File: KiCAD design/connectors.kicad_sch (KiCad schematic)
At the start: 6 parts

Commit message: finished conectors / sensors / converters
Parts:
- added J?: JST BATTERY, Connector_JST:JST_XH_B2B-XH-A_1x02_P2.50mm_Vertical, symbol Connector_Generic:Conn_01x02
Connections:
- net GND: now also J?.1 (Pin_1)
- new net +BATT: J?.2 (Pin_2)
- no-connect marks 9 -> 8
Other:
- note added: "BATTERY"
- company: (none) -> Oulu University
- title: (none) -> Connectors
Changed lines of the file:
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@@
 (kicad_sch (version 20211123) (generator eeschema)
   (paper "A4")
+  (title_block
+    (title "Connectors")
+    (company "Oulu University")
+  )
   (junction (at 50.8 38.1) (diameter 0) (color 0 0 0 0)
   )
@@
   (no_connect (at 38.1 45.72))
   (no_connect (at 50.8 43.18))
-  (no_connect (at 146.05 151.13))
   (no_connect (at 119.38 76.2))
   (no_connect (at 50.8 63.5))
@@
     (stroke (width 0) (type default) (color 0 0 0 0))
   )
+  (polyline (pts (xy 160.02 197.485) (xy 160.655 197.485))
+    (stroke (width 0) (type default) (color 0 0 0 0))
+  )
   (wire (pts (xy 50.8 55.88) (xy 60.96 55.88))
     (stroke (width 0) (type default) (color 0 0 0 0))
@@
     (stroke (width 0) (type default) (color 0 0 0 0))
   )
+  (wire (pts (xy 122.555 148.59) (xy 125.095 148.59))
+    (stroke (width 0) (type default) (color 0 0 0 0))
+  )
   (wire (pts (xy 45.72 55.88) (xy 50.8 55.88))
     (stroke (width 0) (type default) (color 0 0 0 0))
   )
+  (wire (pts (xy 116.205 146.05) (xy 125.095 146.05))
+    (stroke (width 0) (type default) (color 0 0 0 0))
+  )
   (wire (pts (xy 119.38 55.88) (xy 132.08 55.88))
     (stroke (width 0) (type default) (color 0 0 0 0))
   )
+  (wire (pts (xy 122.555 149.86) (xy 122.555 148.59))
+    (stroke (width 0) (type default) (color 0 0 0 0))
+  )
+  (polyline (pts (xy 160.02 109.855) (xy 160.02 197.485))
+    (stroke (width 0) (type default) (color 0 0 0 0))
+  )
   (polyline (pts (xy 101.6 109.22) (xy 101.6 195.58))
     (stroke (width 0) (type default) (color 0 0 0 0))
@@
   )
   (wire (pts (xy 45.72 53.34) (xy 50.8 53.34))
+    (stroke (width 0) (type default) (color 0 0 0 0))
+  )
+  (wire (pts (xy 116.205 144.78) (xy 116.205 146.05))
     (stroke (width 0) (type default) (color 0 0 0 0))
   )
@@
   (text "NUCLEO CONNECTORS" (at 12.7 20.32 0)
     (effects (font (size 4 4)) (justify left bottom))
+  )
+  (text "BATTERY" (at 104.14 116.84 0)
+    (effects (font (size 3.81 3.81)) (justify left bottom))
   )
   (hierarchical_label "PA4" (shape bidirectional) (at 50.8 71.12 0)
@@
     (pin "9")
   )
+  (symbol (lib_id "power:+BATT") (at 116.205 144.78 0) (mirror y) (unit 1)
+    (in_bom yes) (on_board yes) (fields_autoplaced)
+    (property "Reference" "#PWR?" (id 0) (at 116.205 148.59 0)
+      (effects (font (size 1.27 1.27)) hide)
+    )
+    (property "Value" "+BATT" (id 1) (at 116.205 139.7 0))
+    (property "Footprint" "" (id 2) (at 116.205 144.78 0)
+      (effects (font (size 1.27 1.27)) hide)
+    )
+    (property "Datasheet" "" (id 3) (at 116.205 144.78 0)
+      (effects (font (size 1.27 1.27)) hide)
+    )
+    (pin "1")
+  )
   (symbol (lib_id "Connector_Generic:Conn_01x06") (at 203.2 58.42 0) (unit 1)
     (in_bom yes) (on_board yes) (fields_autoplaced)
@@
     (pin "1")
   )
+  (symbol (lib_id "Connector_Generic:Conn_01x02") (at 130.175 148.59 0) (mirror x) (unit 1)
+    (in_bom yes) (on_board yes)
+    (property "Reference" "J?" (id 0) (at 132.715 148.5901 0)
+      (effects (font (size 1.27 1.27)) (justify left))
+    )
+    (property "Value" "JST BATTERY" (id 1) (at 125.095 142.24 0)
+      (effects (font (size 1.27 1.27)) (justify left))
+    )
+    (property "Footprint" "Connector_JST:JST_XH_B2B-XH-A_1x02_P2.50mm_Vertical" (id 2) (at 130.175 148.59 0)
+      (effects (font (size 1.27 1.27)) hide)
+    )
+    (property "Datasheet" "~" (id 3) (at 130.175 148.59 0)
+      (effects (font (size 1.27 1.27)) hide)
+    )
+    (pin "1")
+    (pin "2")
+  )
   (symbol (lib_id "power:+5V") (at 66.04 55.88 180) (unit 1)
     (in_bom yes) (on_board yes) (fields_autoplaced)
@@
     (pin "1")
   )
+  (symbol (lib_id "power:GND") (at 122.555 149.86 0) (mirror y) (unit 1)
+    (in_bom yes) (on_board yes) (fields_autoplaced)
+    (property "Reference" "#PWR?" (id 0) (at 122.555 156.21 0)
+      (effects (font (size 1.27 1.27)) hide)
+    )
+    (property "Value" "GND" (id 1) (at 122.555 154.94 0))
+    (property "Footprint" "" (id 2) (at 122.555 149.86 0)
+      (effects (font (size 1.27 1.27)) hide)
+    )
+    (property "Datasheet" "" (id 3) (at 122.555 149.86 0)
+      (effects (font (size 1.27 1.27)) hide)
+    )
+    (pin "1")
+  )
   (symbol (lib_id "power:GND") (at 132.08 73.66 0) (unit 1)
     (in_bom yes) (on_board yes) (fields_autoplaced)
@@
     (pin "3")
   )
-  (symbol (lib_name "+3.3V_1") (lib_id "power:+3.3V") (at 146.05 151.13 0) (mirror y) (unit 1)
-    (in_bom yes) (on_board yes) (fields_autoplaced)
-    (property "Reference" "#PWR?" (id 0) (at 146.05 154.94 0)
-      (effects (font (size 1.27 1.27)) hide)
-    )
-    (property "Value" "+3.3V" (id 1) (at 146.05 146.05 0))
-    (property "Footprint" "" (id 2) (at 146.05 151.13 0)
-      (effects (font (size 1.27 1.27)) hide)
-    )
-    (property "Datasheet" "" (id 3) (at 146.05 151.13 0)
-      (effects (font (size 1.27 1.27)) hide)
-    )
-    (pin "1")
-  )
   (symbol (lib_id "power:+5V") (at 193.04 52.07 0) (unit 1)

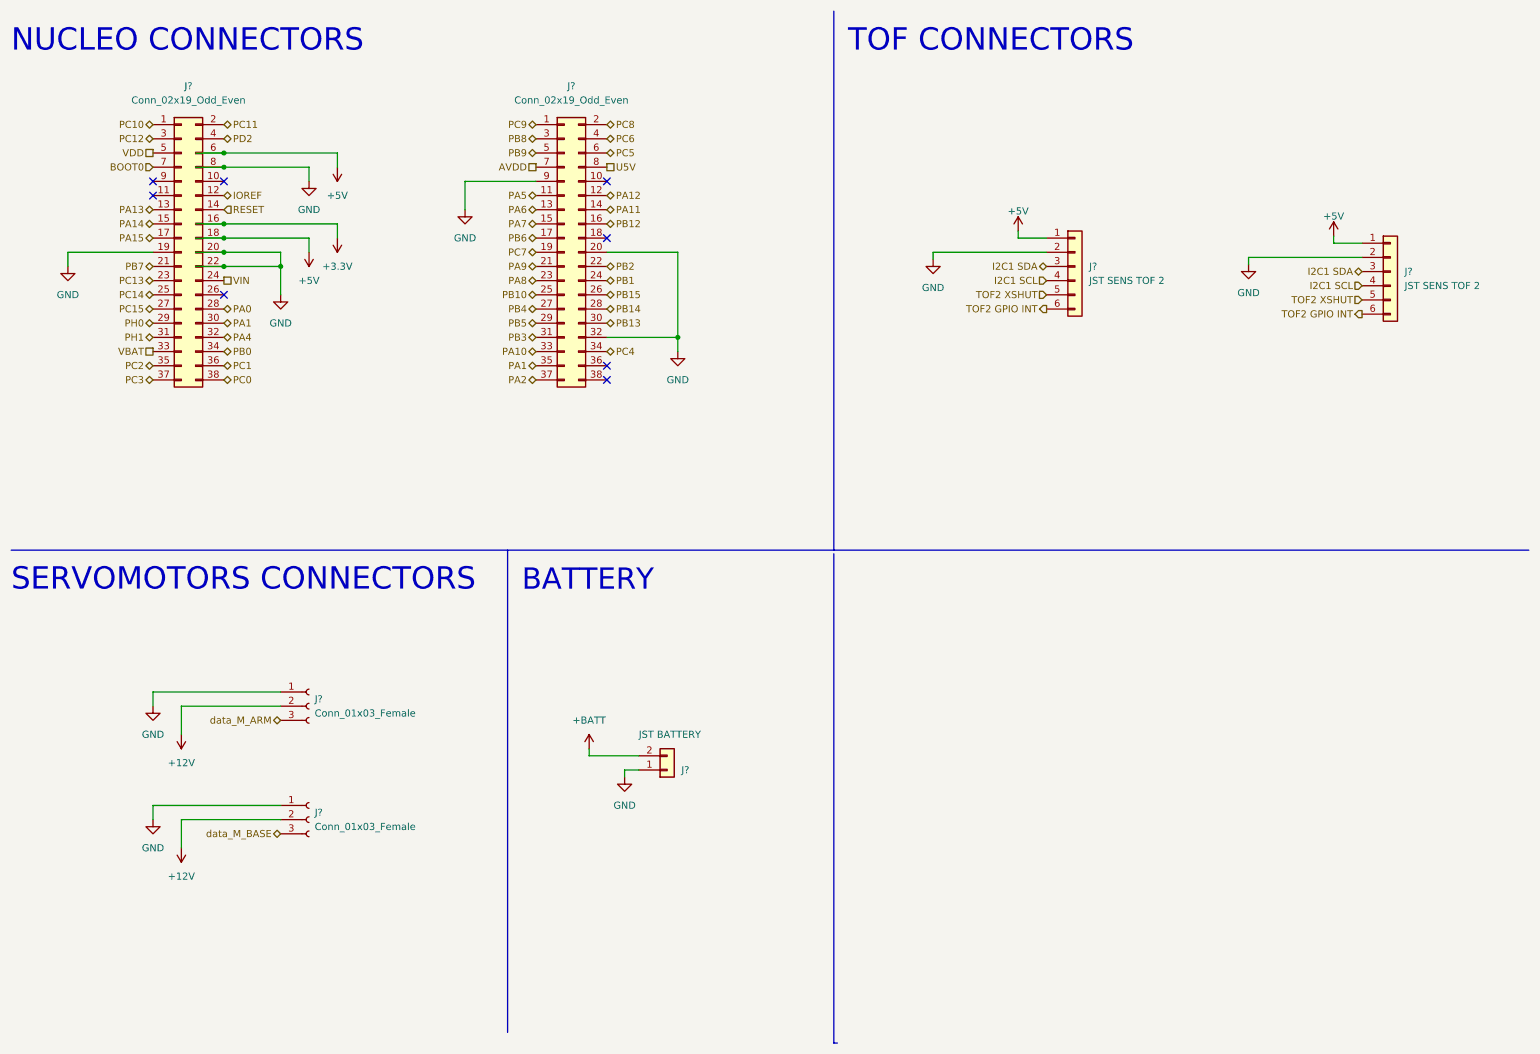
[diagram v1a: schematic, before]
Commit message: labeling and add of components. STM32 pin selected
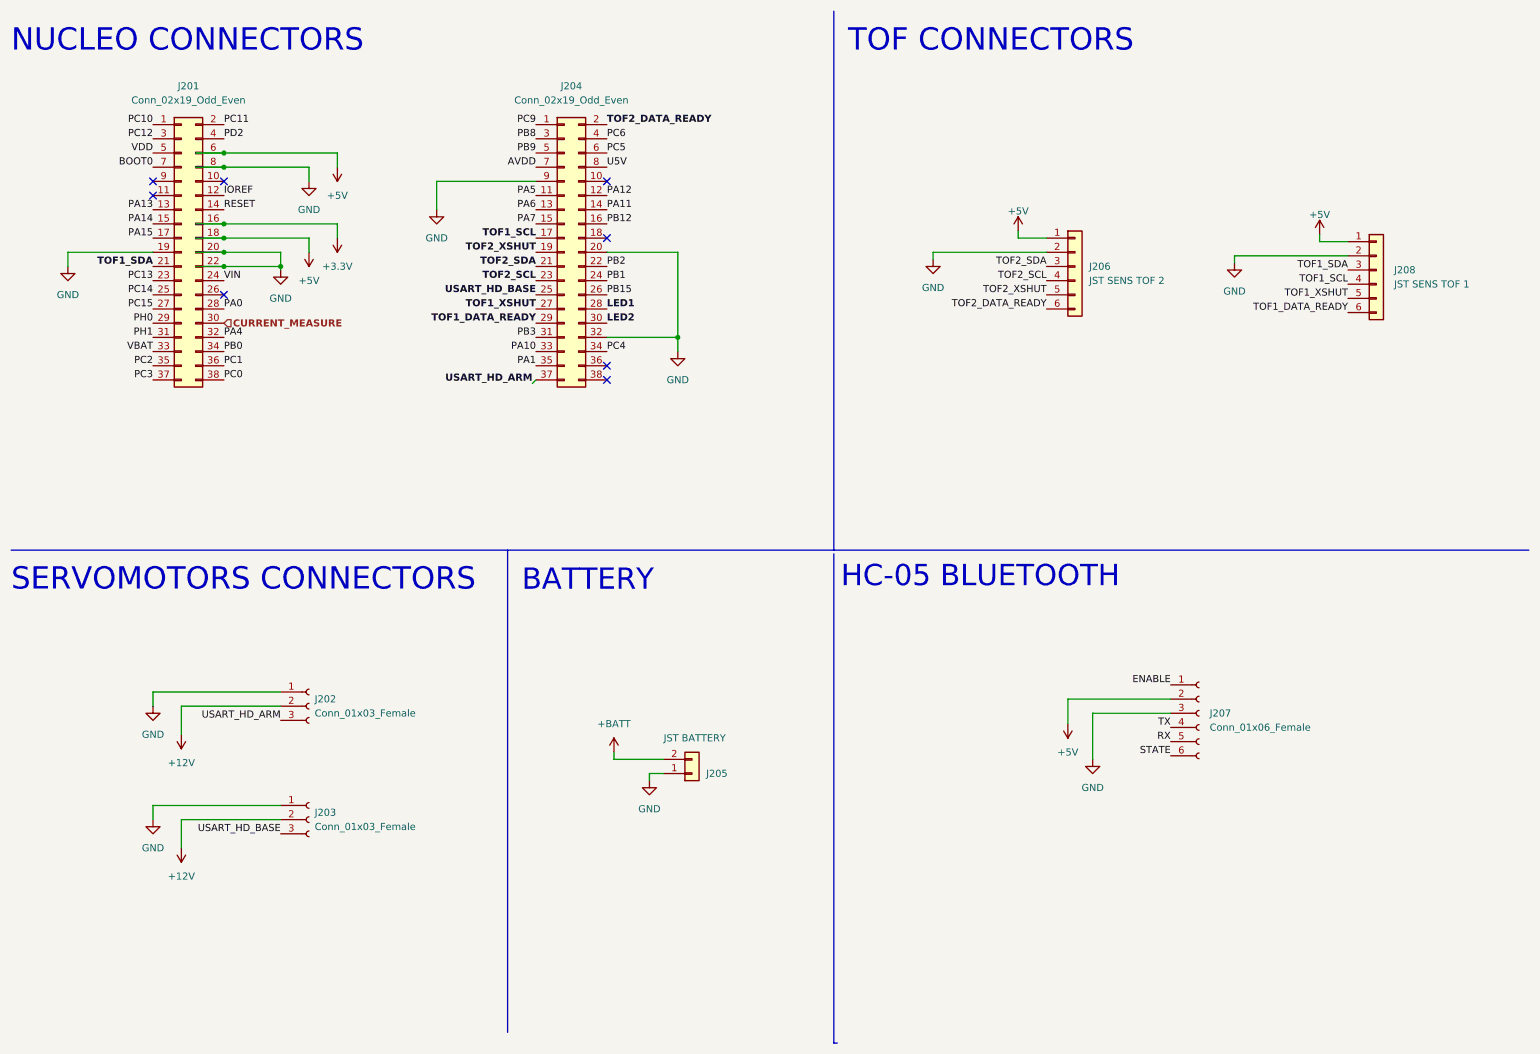
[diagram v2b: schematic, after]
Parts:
- removed J?: JST SENS TOF 2, Connector_JST:JST_XH_B6B-XH-A_1x06_P2.50mm_Vertical, symbol Connector_Generic:Conn_01x06
- added J207: Conn_01x06_Female, symbol Connector:Conn_01x06_Female
- added J208: JST SENS TOF 1, Connector_JST:JST_XH_B6B-XH-A_1x06_P2.50mm_Vertical, symbol Connector_Generic:Conn_01x06
- gave numbers to parts that had none: 6
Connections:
- net PA8 is gone; now on net TOF2_SCL: J204.23 (Pin_23)
- net PA9 is gone; now on net TOF2_SDA: J204.21 (Pin_21)
- net TOF2 GPIO INT is gone; now on net TOF2_DATA_READY: J206.6 (Pin_6)
- net TOF2 XSHUT is gone; now on net TOF2_XSHUT: J206.5 (Pin_5)
- net data_M_ARM is gone; now on net USART_HD_ARM: J202.3 (Pin_3)
- net data_M_BASE is gone; now on net USART_HD_BASE: J203.3 (Pin_3)
- net +5V: now also J207.2 (Pin_2), J208.1 (Pin_1)
- net GND: now also J207.3 (Pin_3), J208.2 (Pin_2)
- net PA1: no longer J201.30 (Pin_30)
- net I2C1 SCL renamed TOF2_SCL
- net I2C1 SDA renamed TOF2_SDA
- net PA2 renamed USART_HD_ARM
- net PB10 renamed USART_HD_BASE
- net PB13 renamed LED2
- net PB14 renamed LED1
- net PB4 renamed TOF1_XSHUT
- net TOF1_XSHUT: now also J208.5 (Pin_5)
- net PB5 renamed TOF1_DATA_READY
- net TOF1_DATA_READY: now also J208.6 (Pin_6)
- net PB6 renamed TOF1_SCL
- net TOF1_SCL: now also J208.4 (Pin_4)
- net PB7 renamed TOF1_SDA
- net TOF1_SDA: now also J208.3 (Pin_3)
- net PC7 renamed TOF2_XSHUT
- net PC8 renamed TOF2_DATA_READY
- new net CURRENT_MEASURE: J201.30 (Pin_30)
- new net ENABLE: J207.1 (Pin_1)
- new net RX: J207.5 (Pin_5)
- new net STATE: J207.6 (Pin_6)
- new net TX: J207.4 (Pin_4)
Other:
- note added: "HC-05 BLUETOOTH"
- moved on the sheet: J205

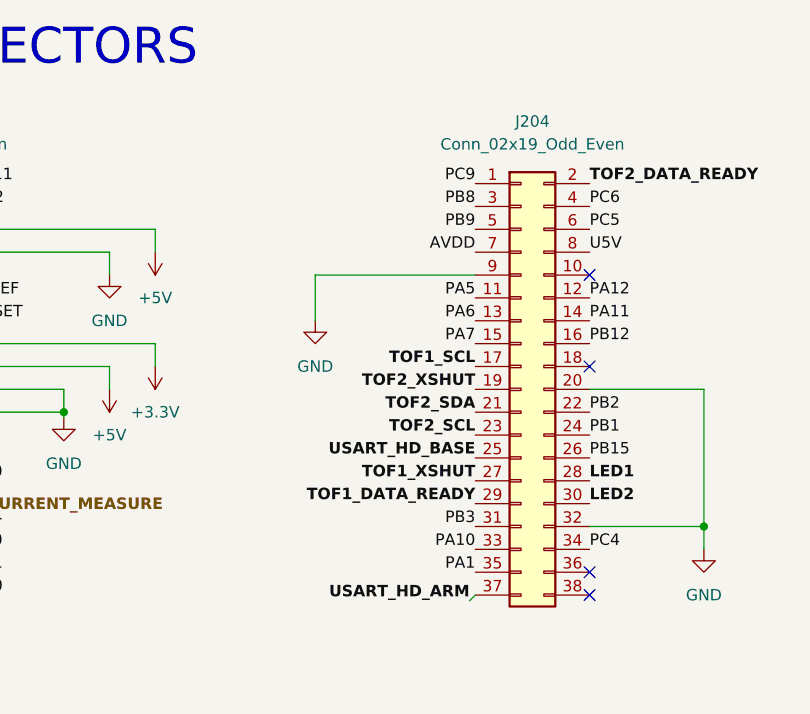
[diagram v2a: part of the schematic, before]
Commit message: correction pin bluetooth
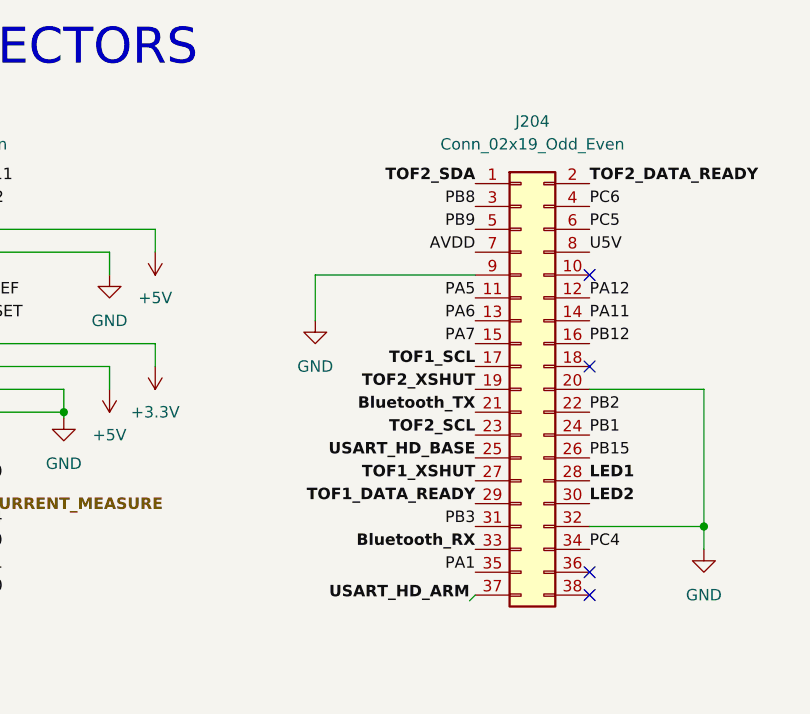
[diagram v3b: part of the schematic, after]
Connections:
- net PC9 is gone; now on net TOF2_SDA: J204.1 (Pin_1)
- net TOF2_SDA: no longer J204.21 (Pin_21)
- net PA10 renamed Bluetooth_RX
- new net Bluetooth_TX: J204.21 (Pin_21)
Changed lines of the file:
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@@
     (effects (font (size 1.27 1.27) (thickness 0.254) bold) (justify left bottom))
   )
-  (label "TOF2_SDA" (at 106.68 58.42 180)
-    (effects (font (size 1.27 1.27) (thickness 0.254) bold) (justify right bottom))
+  (label "Bluetooth_RX" (at 106.68 73.66 180)
+    (effects (font (size 1.27 1.27) bold) (justify right bottom))
   )
   (label "USART_HD_ARM" (at 60.96 139.7 180)
@@
     (effects (font (size 1.27 1.27)) (justify right bottom))
   )
+  (label "Bluetooth_TX" (at 106.68 58.42 180)
+    (effects (font (size 1.27 1.27) (thickness 0.254) bold) (justify right bottom))
+  )
   (label "PA11" (at 119.38 48.26 0)
     (effects (font (size 1.27 1.27)) (justify left bottom))
@@
     (effects (font (size 1.27 1.27)) (justify right bottom))
   )
-  (label "PC9" (at 106.68 33.02 180)
-    (effects (font (size 1.27 1.27)) (justify right bottom))
-  )
   (label "PC10" (at 38.1 33.02 180)
     (effects (font (size 1.27 1.27)) (justify right bottom))
@@
   (label "PC1" (at 50.8 76.2 0)
     (effects (font (size 1.27 1.27)) (justify left bottom))
-  )
-  (label "PA10" (at 106.68 73.66 180)
-    (effects (font (size 1.27 1.27)) (justify right bottom))
   )
   (label "PH1" (at 38.1 71.12 180)
@@
     (effects (font (size 1.27 1.27)) (justify right bottom))
   )
+  (label "TOF2_SDA" (at 106.68 33.02 180)
+    (effects (font (size 1.27 1.27) (thickness 0.254) bold) (justify right bottom))
+  )
   (hierarchical_label "CURRENT_MEASURE" (shape input) (at 50.8 68.58 0)

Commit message: correction of errors
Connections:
- net +5V: no longer J201.18 (Pin_18)
- net +3.3V: no longer names the net of J201.16 (Pin_16)
- net +BATT renamed BATT
- no-connect marks 8 -> 10
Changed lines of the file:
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@@
   (junction (at 50.8 58.42) (diameter 0) (color 0 0 0 0)
   )
-  (junction (at 50.8 53.34) (diameter 0) (color 0 0 0 0)
-  )
   (junction (at 132.08 71.12) (diameter 0) (color 0 0 0 0)
-  )
-  (junction (at 50.8 50.8) (diameter 0) (color 0 0 0 0)
   )
   (junction (at 60.96 58.42) (diameter 0) (color 0 0 0 0)
@@
   (no_connect (at 38.1 43.18))
   (no_connect (at 38.1 45.72))
+  (no_connect (at 50.8 50.8))
   (no_connect (at 50.8 43.18))
   (no_connect (at 119.38 76.2))
   (no_connect (at 50.8 63.5))
   (no_connect (at 119.38 43.18))
+  (no_connect (at 50.8 53.34))
   (no_connect (at 119.38 53.34))
   (wire (pts (xy 43.18 162.56) (xy 43.18 157.48))
@@
     (stroke (width 0) (type default) (color 0 0 0 0))
   )
-  (wire (pts (xy 50.8 50.8) (xy 71.12 50.8))
-    (stroke (width 0) (type default) (color 0 0 0 0))
-  )
   (wire (pts (xy 60.96 134.62) (xy 38.1 134.62))
     (stroke (width 0) (type default) (color 0 0 0 0))
@@
     (stroke (width 0) (type default) (color 0 0 0 0))
   )
-  (wire (pts (xy 66.04 53.34) (xy 66.04 55.88))
-    (stroke (width 0) (type default) (color 0 0 0 0))
-  )
   (wire (pts (xy 60.96 55.88) (xy 60.96 58.42))
     (stroke (width 0) (type default) (color 0 0 0 0))
@@
     (stroke (width 0) (type default) (color 0 0 0 0))
   )
-  (wire (pts (xy 71.12 53.34) (xy 71.12 50.8))
-    (stroke (width 0) (type default) (color 0 0 0 0))
-  )
   (wire (pts (xy 206.375 138.43) (xy 220.345 138.43))
     (stroke (width 0) (type default) (color 0 0 0 0))
@@
   )
   (wire (pts (xy 193.04 53.34) (xy 193.04 52.07))
-    (stroke (width 0) (type default) (color 0 0 0 0))
-  )
-  (wire (pts (xy 50.8 53.34) (xy 66.04 53.34))
     (stroke (width 0) (type default) (color 0 0 0 0))
   )
@@
     (effects (font (size 1.27 1.27)) (justify left bottom))
   )
-  (label "LED2" (at 119.38 68.58 0)
-    (effects (font (size 1.27 1.27) (thickness 0.254) bold) (justify left bottom))
-  )
   (label "PB3" (at 106.68 71.12 180)
     (effects (font (size 1.27 1.27)) (justify right bottom))
@@
   (label "VBAT" (at 38.1 73.66 180)
     (effects (font (size 1.27 1.27)) (justify right bottom))
-  )
-  (label "LED1" (at 119.38 66.04 0)
-    (effects (font (size 1.27 1.27) (thickness 0.254) bold) (justify left bottom))
   )
   (label "TOF2_DATA_READY" (at 119.38 33.02 0)
@@
     (effects (font (size 1.27 1.27) (thickness 0.254) bold) (justify right bottom))
   )
+  (hierarchical_label "BATT" (shape input) (at 120.65 145.415 90)
+    (effects (font (size 1.27 1.27) bold) (justify left))
+  )
+  (hierarchical_label "LED2" (shape input) (at 119.38 68.58 0)
+    (effects (font (size 1.27 1.27) (thickness 0.254) bold) (justify left))
+  )
   (hierarchical_label "CURRENT_MEASURE" (shape input) (at 50.8 68.58 0)
+    (effects (font (size 1.27 1.27) (thickness 0.254) bold) (justify left))
+  )
+  (hierarchical_label "LED1" (shape input) (at 119.38 66.04 0)
     (effects (font (size 1.27 1.27) (thickness 0.254) bold) (justify left))
   )
@@
     )
     (property "Datasheet" "" (id 3) (at 88.9 48.26 0)
-      (effects (font (size 1.27 1.27)) hide)
-    )
-    (pin "1")
-  )
-  (symbol (lib_id "power:+3.3V") (at 71.12 53.34 180) (unit 1)
-    (in_bom yes) (on_board yes) (fields_autoplaced)
-    (property "Reference" "#PWR0210" (id 0) (at 71.12 49.53 0)
-      (effects (font (size 1.27 1.27)) hide)
-    )
-    (property "Value" "+3.3V" (id 1) (at 71.12 58.42 0))
-    (property "Footprint" "" (id 2) (at 71.12 53.34 0)
-      (effects (font (size 1.27 1.27)) hide)
-    )
-    (property "Datasheet" "" (id 3) (at 71.12 53.34 0)
       (effects (font (size 1.27 1.27)) hide)
     )
@@
     (pin "9")
   )
-  (symbol (lib_id "power:+BATT") (at 120.65 145.415 0) (mirror y) (unit 1)
-    (in_bom yes) (on_board yes) (fields_autoplaced)
-    (property "Reference" "#PWR0212" (id 0) (at 120.65 149.225 0)
-      (effects (font (size 1.27 1.27)) hide)
-    )
-    (property "Value" "+BATT" (id 1) (at 120.65 140.335 0))
-    (property "Footprint" "" (id 2) (at 120.65 145.415 0)
-      (effects (font (size 1.27 1.27)) hide)
-    )
-    (property "Datasheet" "" (id 3) (at 120.65 145.415 0)
-      (effects (font (size 1.27 1.27)) hide)
-    )
-    (pin "1")
-  )
   (symbol (lib_id "Connector_Generic:Conn_01x06") (at 203.2 58.42 0) (unit 1)
     (in_bom yes) (on_board yes) (fields_autoplaced)
@@
     (pin "2")
   )
-  (symbol (lib_id "power:+5V") (at 66.04 55.88 180) (unit 1)
-    (in_bom yes) (on_board yes) (fields_autoplaced)
-    (property "Reference" "#PWR0208" (id 0) (at 66.04 52.07 0)
-      (effects (font (size 1.27 1.27)) hide)
-    )
-    (property "Value" "+5V" (id 1) (at 66.04 60.96 0))
-    (property "Footprint" "" (id 2) (at 66.04 55.88 0)
-      (effects (font (size 1.27 1.27)) hide)
-    )
-    (property "Datasheet" "" (id 3) (at 66.04 55.88 0)
-      (effects (font (size 1.27 1.27)) hide)
-    )
-    (pin "1")
-  )
   (symbol (lib_id "power:+5V") (at 201.93 140.335 180) (unit 1)
